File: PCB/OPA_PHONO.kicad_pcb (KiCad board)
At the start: 4 copper layers, 99.5 x 15 mm, 64 parts, among them J1 PJRAS2X1S01X, J2 PJRAS2X1S01X, J3 UJC-HP-3-SMT-TR, U1 OPA1644AxD, U2 OPA1612AxD, U3 LTC3265xDHC

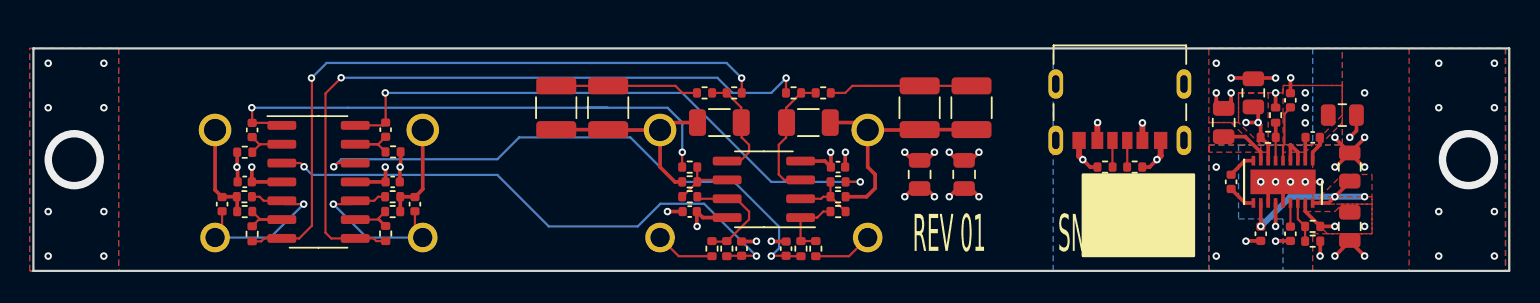
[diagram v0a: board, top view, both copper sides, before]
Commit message: differential amp initial changes
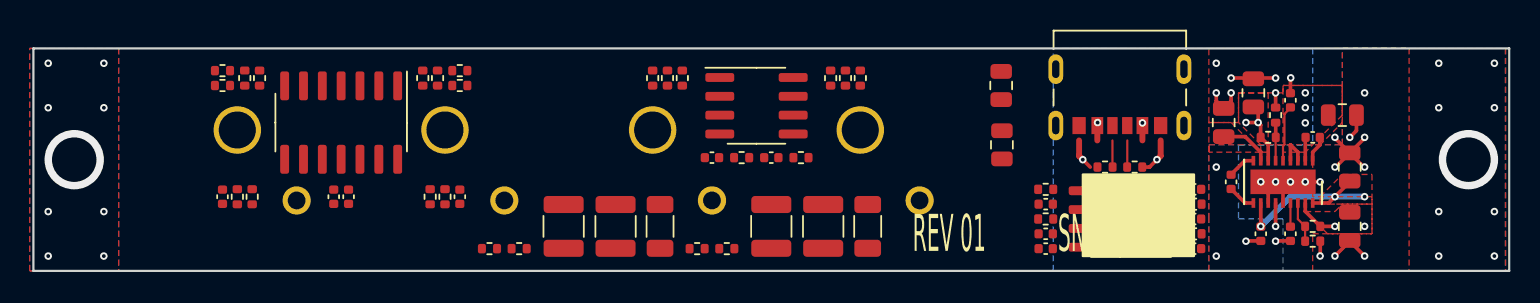
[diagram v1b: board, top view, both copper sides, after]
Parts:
- added C29: 1u, Capacitor_SMD:C_0402_1005Metric, F.Cu at (178.5, 59.5)
- added C30: 1u, Capacitor_SMD:C_0402_1005Metric, F.Cu at (168.5, 63.5)
- added R18: 16k, Resistor_SMD:R_0402_1005Metric, F.Cu at (115.5, 52.0)
- added R20: 499R, Resistor_SMD:R_0402_1005Metric, F.Cu at (113.0, 52.5)
- added R31: 16k, Resistor_SMD:R_0402_1005Metric, F.Cu at (129.0, 51.5)
- added R32: 16k, Resistor_SMD:R_0402_1005Metric, F.Cu at (127.5, 52.0)
- added R33: 16k, Resistor_SMD:R_0402_1005Metric, F.Cu at (126.5, 52.0)
- added R34: 499R, Resistor_SMD:R_0402_1005Metric, F.Cu at (129.0, 52.5)
- added U4: OPA1612AxD, Package_SO:SOIC-8_3.9x4.9mm_P1.27mm, F.Cu at (173.5, 61.5)
- J1, J2: value PJRAS2X1S01X -> RCJ-21XX; footprint OPA_PHONO:PJRAS2X1S01X -> LIB:RCJ-21XX
- R15, R3: value 499R -> 16k
- moved C5 55.1 mm to (178.5, 63.5), turned to 0 degrees
- moved R10 54.3 mm to (178.5, 62.5)
- moved R22 54.2 mm to (168.5, 61.5)
- moved C11 54.0 mm to (168.5, 62.5), turned to 180 degrees
- moved J1 32.7 mm to (121.0, 55.5), turned to 180 degrees
- moved C3 28.6 mm to (136.0, 62.0), turned to 90 degrees
- moved C6 27.6 mm to (178.5, 61.5), turned to 0 degrees
- moved R11 26.7 mm to (178.5, 60.5), turned to 180 degrees
- moved J2 26.3 mm to (149.0, 55.5), turned to 180 degrees
- moved R4 23.0 mm to (131.0, 63.5)
- moved R5 23.0 mm to (133.0, 63.5)
- moved C2 22.0 mm to (139.5, 62.0), turned to 90 degrees
- moved R23 21.9 mm to (168.5, 59.5), turned to 0 degrees
- moved C12 20.7 mm to (168.5, 60.5), turned to 180 degrees
- moved C8 19.7 mm to (153.5, 62.0), turned to 90 degrees
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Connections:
- C1 pad 1: /IN_R -> /RIGHT/INP
- C1 pad 2: GND -> /RIGHT/INN
- C7 pad 1: /IN_L -> /LEFT/INP
- C7 pad 2: GND -> /LEFT/INN
- R1 pad 1: GND -> /RIGHT/INN
- R1 pad 2: /IN_R -> /RIGHT/INP
- R13 pad 1: GND -> /LEFT/INN
- R13 pad 2: /IN_L -> /LEFT/INP
- R14 pad 2: /LEFT/FB1 -> /LEFT/FB1P
- R15 pad 1: GND -> /RIGHT/OUT1B
- R15 pad 2: /LEFT/FB1 -> /RIGHT/FB1N
- R2 pad 2: /RIGHT/FB1 -> /RIGHT/FB1P
- R3 pad 1: GND -> /RIGHT/FB1P
- R3 pad 2: /RIGHT/FB1 -> /RIGHT/OUT1B
- U1 pad 1: /LEFT/TRIM -> /LEFT/OUT1B
- U1 pad 10: /IN_R -> /RIGHT/INP
- U1 pad 12: /RIGHT/OUT_RC -> /LEFT/INP
- U1 pad 13: /RIGHT/FBTRIM -> /LEFT/FB1P
- U1 pad 14: /RIGHT/TRIM -> /LEFT/OUT1
- U1 pad 2: /LEFT/FBTRIM -> /LEFT/FB1N
- U1 pad 3: /LEFT/OUT_RC -> /LEFT/INN
- U1 pad 5: /IN_L -> /RIGHT/INN
- U1 pad 6: /LEFT/FB1 -> /RIGHT/FB1N
- U1 pad 7: /LEFT/OUT1 -> /RIGHT/OUT1B
- U1 pad 9: /RIGHT/FB1 -> /RIGHT/FB1P
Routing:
- net GND: track 86.5 -> 30.5 mm, vias 55 -> 45
- net /RIGHT/OUT1: track 47.0 -> 0.00 mm, vias 2 -> 0
- net /LEFT/OUT1: track 45.3 -> 0.00 mm, vias 2 -> 0
- net /RIGHT/TRIM: track 39.6 -> 0.00 mm, vias 2 -> 0
- net /RIGHT/OUT_RC: track 39.1 -> 0.00 mm, vias 2 -> 0
- net /LEFT/OUT_RC: track 37.9 -> 0.00 mm, vias 2 -> 0
- net /LEFT/TRIM: track 37.0 -> 0.00 mm, vias 2 -> 0
- net /IN_L: track 12.6 -> 0.00 mm, vias 1 -> 0
- net /IN_R: track 11.9 -> 0.00 mm, vias 1 -> 0
- net /RIGHT/RIAA_RC: track 9.69 -> 0.00 mm
- net /LEFT/RIAA_RC: track 9.69 -> 0.00 mm
- net /RIGHT/RIAA: track 8.76 -> 0.00 mm
- net /POWER/-6V: track 13.6 -> 4.87 mm, vias 6 -> 2
- net /POWER/+6V: track 11.7 -> 2.98 mm, vias 6 -> 2
- net /LEFT/OUT2: track 7.56 -> 0.00 mm
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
